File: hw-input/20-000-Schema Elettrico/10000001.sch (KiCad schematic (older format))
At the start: 32 parts

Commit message: Completamento sbroglio hw-output
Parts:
- removed IC? (x2): LTV-358T, MFSOP6, symbol LTV-358T
- added IC1, IC2: TLP291, SOP4, symbol TLP291
- gave numbers to parts that had none: 30
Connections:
- net labels removed: IO_1_L

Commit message: Aggiunte capacità di bypass su alimentazione I2C expander
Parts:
- added C1: 100n, Capacitors_SMD:C_0603, symbol C
- added C2: 1u, Capacitors_SMD:C_0603, symbol C
- IC1, IC2: footprint SOP4 -> (none)
- R1, R2, R3, R4, R5, R6, R7, R8, R9: footprint ~ -> Resistors_SMD:R_0603
- R10, R11, R12, R13, R14, R15, R16, R17, R18, R19: footprint ~ -> (none)
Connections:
- wire segments 115 -> 121
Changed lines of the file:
@@
 LIBS:optocoupler-2
 LIBS:10000001-cache
-EELAYER 27 0
+EELAYER 25 0
 EELAYER END
 $Descr A4 11693 8268
@@
 F 0 "R7" V 4450 1450 40  0000 C CNN
 F 1 "10000" V 4507 1251 40  0000 C CNN
-F 2 "~" V 4430 1250 30  0000 C CNN
+F 2 "Resistors_SMD:R_0603" V 4430 1250 30  0000 C CNN
 F 3 "~" H 4500 1250 30  0000 C CNN
 	1    4500 1250
@@
 F 0 "R8" V 4600 1450 40  0000 C CNN
 F 1 "10000" V 4657 1251 40  0000 C CNN
-F 2 "~" V 4580 1250 30  0000 C CNN
+F 2 "Resistors_SMD:R_0603" V 4580 1250 30  0000 C CNN
 F 3 "~" H 4650 1250 30  0000 C CNN
 	1    4650 1250
@@
 F 0 "R9" V 4750 1450 40  0000 C CNN
 F 1 "10000" V 4807 1251 40  0000 C CNN
-F 2 "~" V 4730 1250 30  0000 C CNN
+F 2 "Resistors_SMD:R_0603" V 4730 1250 30  0000 C CNN
 F 3 "~" H 4800 1250 30  0000 C CNN
 	1    4800 1250
@@
 F 0 "R6" V 2200 6500 40  0000 C CNN
 F 1 "0" V 2157 6701 40  0000 C CNN
-F 2 "~" V 2080 6700 30  0000 C CNN
+F 2 "Resistors_SMD:R_0603" V 2080 6700 30  0000 C CNN
 F 3 "~" H 2150 6700 30  0000 C CNN
 	1    2150 6700
@@
 F 0 "R5" V 2200 6400 40  0000 C CNN
 F 1 "0" V 2157 6601 40  0000 C CNN
-F 2 "~" V 2080 6600 30  0000 C CNN
+F 2 "Resistors_SMD:R_0603" V 2080 6600 30  0000 C CNN
 F 3 "~" H 2150 6600 30  0000 C CNN
 	1    2150 6600
@@
 F 0 "R4" V 2200 6300 40  0000 C CNN
 F 1 "0" V 2157 6501 40  0000 C CNN
-F 2 "~" V 2080 6500 30  0000 C CNN
+F 2 "Resistors_SMD:R_0603" V 2080 6500 30  0000 C CNN
 F 3 "~" H 2150 6500 30  0000 C CNN
 	1    2150 6500
@@
 F 0 "R3" V 2200 6200 40  0000 C CNN
 F 1 "0" V 2157 6401 40  0000 C CNN
-F 2 "~" V 2080 6400 30  0000 C CNN
+F 2 "Resistors_SMD:R_0603" V 2080 6400 30  0000 C CNN
 F 3 "~" H 2150 6400 30  0000 C CNN
 	1    2150 6400
@@
 F 0 "R2" V 2200 6100 40  0000 C CNN
 F 1 "0" V 2157 6301 40  0000 C CNN
-F 2 "~" V 2080 6300 30  0000 C CNN
+F 2 "Resistors_SMD:R_0603" V 2080 6300 30  0000 C CNN
 F 3 "~" H 2150 6300 30  0000 C CNN
 	1    2150 6300
@@
 F 0 "R1" V 2200 6000 40  0000 C CNN
 F 1 "0" V 2157 6201 40  0000 C CNN
-F 2 "~" V 2080 6200 30  0000 C CNN
+F 2 "Resistors_SMD:R_0603" V 2080 6200 30  0000 C CNN
 F 3 "~" H 2150 6200 30  0000 C CNN
 	1    2150 6200
@@
 F 0 "R17" V 7830 5750 40  0000 C CNN
 F 1 "2400" V 7757 5751 40  0000 C CNN
-F 2 "~" V 7680 5750 30  0000 C CNN
+F 2 "" V 7680 5750 30  0000 C CNN
 F 3 "~" H 7750 5750 30  0000 C CNN
 	1    7750 5750
@@
 F 0 "R19" V 8380 5750 40  0000 C CNN
 F 1 "2400" V 8307 5751 40  0000 C CNN
-F 2 "~" V 8230 5750 30  0000 C CNN
+F 2 "" V 8230 5750 30  0000 C CNN
 F 3 "~" H 8300 5750 30  0000 C CNN
 	1    8300 5750
@@
 F 0 "R15" V 7530 6050 40  0000 C CNN
 F 1 "100" V 7457 6051 40  0000 C CNN
-F 2 "~" V 7380 6050 30  0000 C CNN
+F 2 "" V 7380 6050 30  0000 C CNN
 F 3 "~" H 7450 6050 30  0000 C CNN
 	1    7450 6050
@@
 F 0 "R14" V 7530 4300 40  0000 C CNN
 F 1 "100" V 7457 4301 40  0000 C CNN
-F 2 "~" V 7380 4300 30  0000 C CNN
+F 2 "" V 7380 4300 30  0000 C CNN
 F 3 "~" H 7450 4300 30  0000 C CNN
 	1    7450 4300
@@
 F 0 "R18" V 8380 4000 40  0000 C CNN
 F 1 "2400" V 8307 4001 40  0000 C CNN
-F 2 "~" V 8230 4000 30  0000 C CNN
+F 2 "" V 8230 4000 30  0000 C CNN
 F 3 "~" H 8300 4000 30  0000 C CNN
 	1    8300 4000
@@
 F 0 "R16" V 7830 4000 40  0000 C CNN
 F 1 "2400" V 7757 4001 40  0000 C CNN
-F 2 "~" V 7680 4000 30  0000 C CNN
+F 2 "" V 7680 4000 30  0000 C CNN
 F 3 "~" H 7750 4000 30  0000 C CNN
 	1    7750 4000
@@
 F 0 "R12" V 6480 5450 40  0000 C CNN
 F 1 "1000" V 6407 5451 40  0000 C CNN
-F 2 "~" V 6330 5450 30  0000 C CNN
+F 2 "" V 6330 5450 30  0000 C CNN
 F 3 "~" H 6400 5450 30  0000 C CNN
 	1    6400 5450
@@
 F 0 "R13" V 6480 6050 40  0000 C CNN
 F 1 "10000" V 6407 6051 40  0000 C CNN
-F 2 "~" V 6330 6050 30  0000 C CNN
+F 2 "" V 6330 6050 30  0000 C CNN
 F 3 "~" H 6400 6050 30  0000 C CNN
 	1    6400 6050
@@
 F 0 "R11" V 6480 4300 40  0000 C CNN
 F 1 "10000" V 6407 4301 40  0000 C CNN
-F 2 "~" V 6330 4300 30  0000 C CNN
+F 2 "" V 6330 4300 30  0000 C CNN
 F 3 "~" H 6400 4300 30  0000 C CNN
 	1    6400 4300
@@
 F 0 "R10" V 6480 3700 40  0000 C CNN
 F 1 "1000" V 6407 3701 40  0000 C CNN
-F 2 "~" V 6330 3700 30  0000 C CNN
+F 2 "" V 6330 3700 30  0000 C CNN
 F 3 "~" H 6400 3700 30  0000 C CNN
 	1    6400 3700
@@
 F 0 "IC1" H 6787 4278 40  0000 C CNN
 F 1 "TLP291" H 7149 3916 40  0000 C CNN
-F 2 "SOP4" H 6836 3926 29  0000 C CNN
+F 2 "" H 6836 3926 29  0000 C CNN
 F 3 "" H 7000 4100 60  0000 C CNN
 	1    7000 4100
@@
 F 0 "IC2" H 6787 6028 40  0000 C CNN
 F 1 "TLP291" H 7149 5666 40  0000 C CNN
-F 2 "SOP4" H 6836 5676 29  0000 C CNN
+F 2 "" H 6836 5676 29  0000 C CNN
 F 3 "" H 7000 5850 60  0000 C CNN
 	1    7000 5850
 	-1   0    0    -1
 $EndComp
+$Comp
+L C C2
+U 1 1 55357ECE
+P 3200 1200
+F 0 "C2" H 3250 1300 50  0000 L CNN
+F 1 "1u" H 3250 1100 50  0000 L CNN
+F 2 "Capacitors_SMD:C_0603" H 3238 1050 30  0001 C CNN
+F 3 "" H 3200 1200 60  0000 C CNN
+	1    3200 1200
+	1    0    0    -1
+$EndComp
+$Comp
+L C C1
+U 1 1 55357FCD
+P 2900 1200
+F 0 "C1" H 2950 1300 50  0000 L CNN
+F 1 "100n" H 2950 1100 50  0000 L CNN
+F 2 "Capacitors_SMD:C_0603" H 2938 1050 30  0001 C CNN
+F 3 "" H 2900 1200 60  0000 C CNN
+	1    2900 1200
+	1    0    0    -1
+$EndComp
+$Comp
+L GND #PWR017
+U 1 1 5535805C
+P 2900 1550
+F 0 "#PWR017" H 2900 1550 30  0001 C CNN
+F 1 "GND" H 2900 1480 30  0001 C CNN
+F 2 "" H 2900 1550 60  0001 C CNN
+F 3 "" H 2900 1550 60  0001 C CNN
+	1    2900 1550
+	1    0    0    -1
+$EndComp
+$Comp
+L VDD #PWR018
+U 1 1 55358089
+P 2900 800
+F 0 "#PWR018" H 2900 900 30  0001 C CNN
+F 1 "VDD" H 2900 910 30  0000 C CNN
+F 2 "" H 2900 800 60  0001 C CNN
+F 3 "" H 2900 800 60  0001 C CNN
+	1    2900 800
+	1    0    0    -1
+$EndComp
+Wire Wire Line
+	2900 800  2900 1000
+Wire Wire Line
+	2900 900  3200 900
+Wire Wire Line
+	3200 900  3200 1000
+Connection ~ 2900 900
+Wire Wire Line
+	2900 1400 2900 1550
+Wire Wire Line
+	2900 1500 3200 1500
+Wire Wire Line
+	3200 1500 3200 1400
+Connection ~ 2900 1500
 $EndSCHEMATC

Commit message: Aggiornato schema scheda temperatura a nuova versione kicad. Aggiunti script e librerie per generazione diretta BOM con codici d'ordine.
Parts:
- C1, C2: symbol C -> C-RESCUE-10000001
- D1, D2: symbol ZENERSMALL -> ZENERsmall
- IC1, IC2: symbol TLP291 -> TLP291-RESCUE-10000001
- R1, R10, R11, R12, R13, R14, R15, R16, R17, R18, R19, R2, R3, R4, R5, R6, R7, R8, R9: symbol R -> R-RESCUE-10000001
- U1: symbol PCF8574 -> PCF8574-RESCUE-10000001
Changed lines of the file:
@@
 EESchema Schematic File Version 2
+LIBS:10000001-rescue
 LIBS:opto
 LIBS:power
@@
 LIBS:memory
 LIBS:xilinx
-LIBS:special
 LIBS:microcontrollers
 LIBS:dsp
@@
 LIBS:contrib
 LIBS:valves
-LIBS:AQZ204
 LIBS:ftdi
-LIBS:optocoupler
-LIBS:optocoupler-2
 LIBS:10000001-cache
 EELAYER 25 0
@@
 	9800 6100 9800 6150
 $Comp
-L ZENERSMALL D2
+L ZENERsmall D2
 U 1 1 547BA3D0
 P 9800 6250
@@
 IO_0_P
 $Comp
-L ZENERSMALL D1
+L ZENERsmall D1
 U 1 1 547BA3A6
 P 9800 5800
@@
 I2C_SCL
 $Comp
-L R R7
+L R-RESCUE-10000001 R7
 U 1 1 547BA201
 P 4500 1250
@@
 $EndComp
 $Comp
-L R R8
+L R-RESCUE-10000001 R8
 U 1 1 547BA1FE
 P 4650 1250
@@
 $EndComp
 $Comp
-L R R9
+L R-RESCUE-10000001 R9
 U 1 1 547BA1E9
 P 4800 1250
@@
 $EndComp
 $Comp
-L PCF8574 U1
+L PCF8574-RESCUE-10000001 U1
 U 1 1 547BA1C7
 P 5800 2000
@@
 IO_1_CMD
 $Comp
-L R R6
+L R-RESCUE-10000001 R6
 U 1 1 547BA02B
 P 2150 6700
@@
 $EndComp
 $Comp
-L R R5
+L R-RESCUE-10000001 R5
 U 1 1 547BA026
 P 2150 6600
@@
 $EndComp
 $Comp
-L R R4
+L R-RESCUE-10000001 R4
 U 1 1 547BA01C
 P 2150 6500
@@
 $EndComp
 $Comp
-L R R3
+L R-RESCUE-10000001 R3
 U 1 1 547BA018
 P 2150 6400
@@
 $EndComp
 $Comp
-L R R2
+L R-RESCUE-10000001 R2
 U 1 1 547B9FFD
 P 2150 6300
@@
 $EndComp
 $Comp
-L R R1
+L R-RESCUE-10000001 R1
 U 1 1 547B9FF3
 P 2150 6200
@@
 IO_1_N
 $Comp
-L R R17
+L R-RESCUE-10000001 R17
 U 1 1 547B9E50
 P 7750 5750
@@
 $EndComp
 $Comp
-L R R19
+L R-RESCUE-10000001 R19
 U 1 1 547B9E4F
 P 8300 5750
@@
 $EndComp
 $Comp
-L R R15
+L R-RESCUE-10000001 R15
 U 1 1 547B9E4E
 P 7450 6050
@@
 $EndComp
 $Comp
-L R R14
+L R-RESCUE-10000001 R14
 U 1 1 547B9DEF
 P 7450 4300
@@
 $EndComp
 $Comp
-L R R18
+L R-RESCUE-10000001 R18
 U 1 1 547B9DDC
 P 8300 4000
@@
 $EndComp
 $Comp
-L R R16
+L R-RESCUE-10000001 R16
 U 1 1 547B9DBB
 P 7750 4000
@@
 $EndComp
 $Comp
-L R R12
+L R-RESCUE-10000001 R12
 U 1 1 547B9BC6
 P 6400 5450
@@
 $EndComp
 $Comp
-L R R13
+L R-RESCUE-10000001 R13
 U 1 1 547B9BC3
 P 6400 6050
@@
 $EndComp
 $Comp
-L R R11
+L R-RESCUE-10000001 R11
 U 1 1 547B9AAC
 P 6400 4300
@@
 IO_1_N
 $Comp
-L R R10
+L R-RESCUE-10000001 R10
 U 1 1 5456065C
 P 6400 3700
@@
 Protezioni lato utente
 $Comp
-L TLP291 IC1
+L TLP291-RESCUE-10000001 IC1
 U 1 1 54E9B476
 P 7000 4100
@@
 $EndComp
 $Comp
-L TLP291 IC2
+L TLP291-RESCUE-10000001 IC2
 U 1 1 54E9B4A1
 P 7000 5850
@@
 $EndComp
 $Comp
-L C C2
+L C-RESCUE-10000001 C2
 U 1 1 55357ECE
 P 3200 1200
@@
 $EndComp
 $Comp
-L C C1
+L C-RESCUE-10000001 C1
 U 1 1 55357FCD
 P 2900 1200

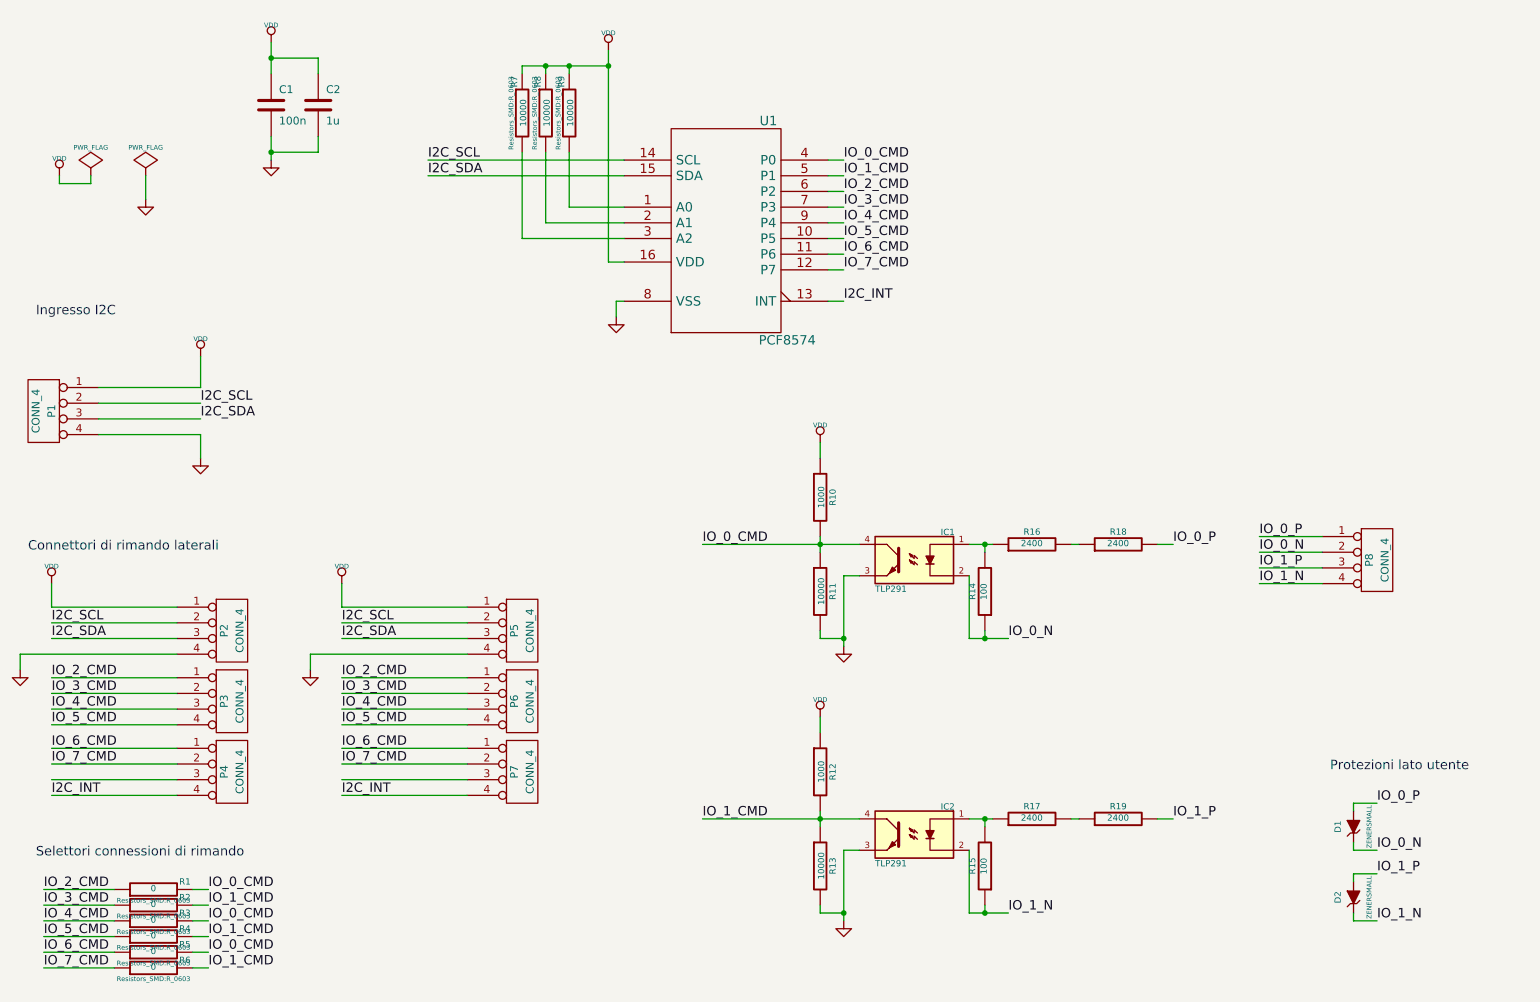
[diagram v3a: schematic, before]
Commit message: Completato schema elettrico con codice produttore
Signed-off-by: CrazyDiamond <crazyd14@gmail.com>
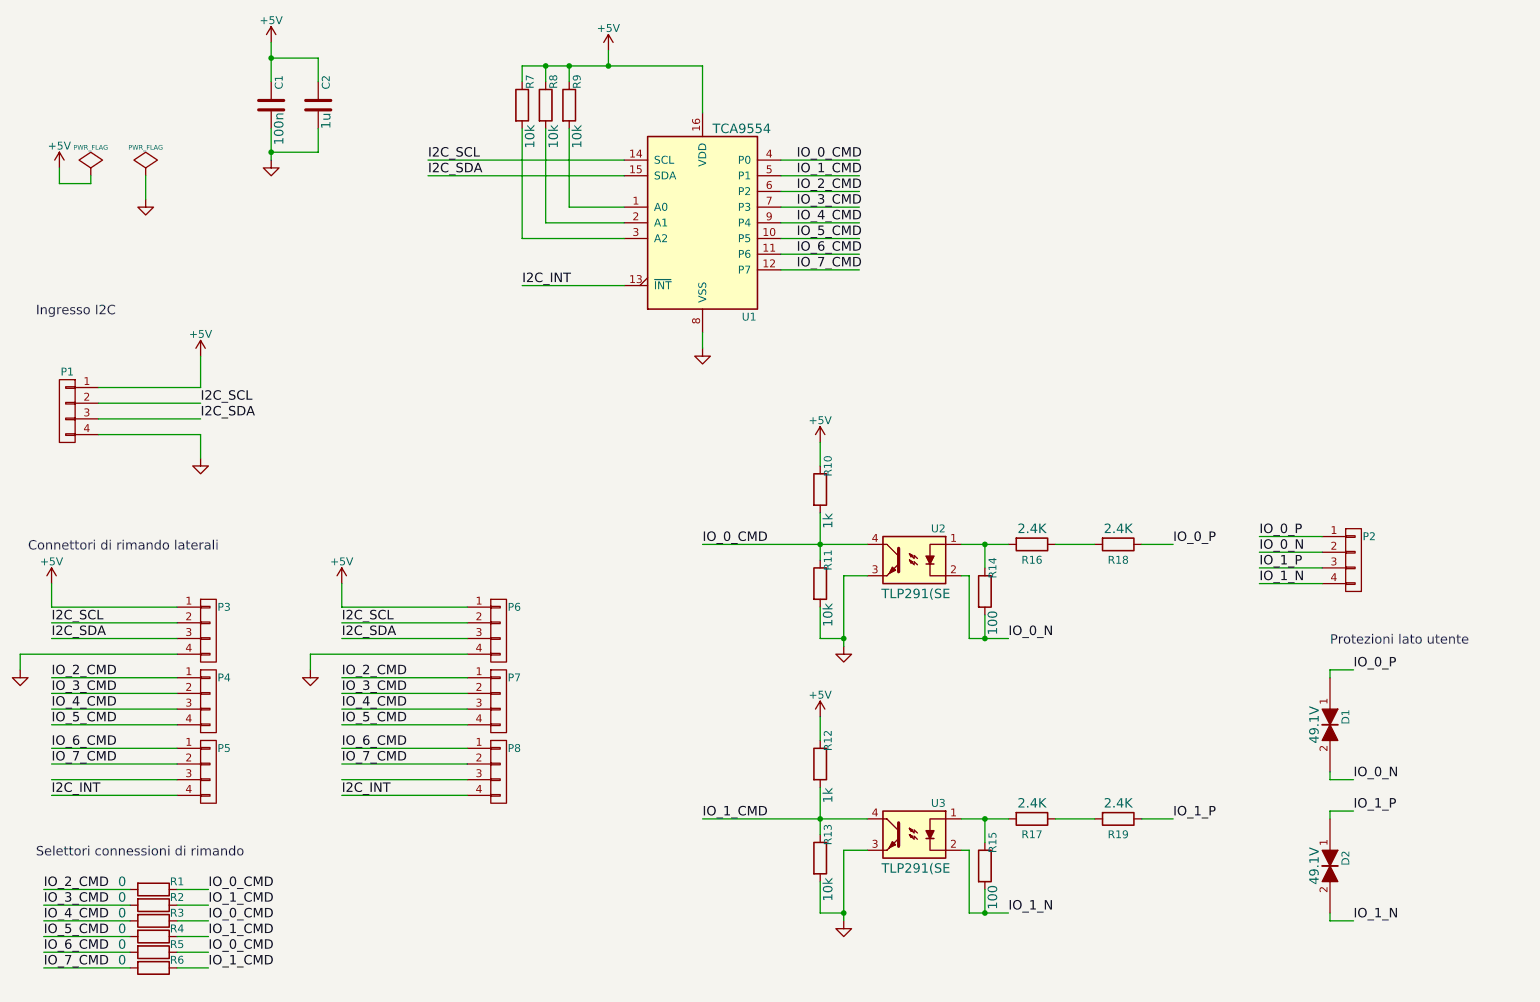
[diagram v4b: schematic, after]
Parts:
- removed C1: 100n, Capacitors_SMD:C_0603, symbol C-RESCUE-10000001
- removed C2: 1u, Capacitors_SMD:C_0603, symbol C-RESCUE-10000001
- removed D1, D2: ZENERSMALL, symbol ZENERsmall
- removed IC1, IC2: TLP291, symbol TLP291-RESCUE-10000001
- removed P1, P2, P3, P4, P5, P6, P7, P8: CONN_4, symbol CONN_4
- removed R1, R2, R3, R4, R5, R6: 0, Resistors_SMD:R_0603, symbol R-RESCUE-10000001
- removed R10, R12: 1000, symbol R-RESCUE-10000001
- removed R11, R13: 10000, symbol R-RESCUE-10000001
- removed R14, R15: 100, symbol R-RESCUE-10000001
- removed R16, R17, R18, R19: 2400, symbol R-RESCUE-10000001
- removed R7, R8, R9: 10000, Resistors_SMD:R_0603, symbol R-RESCUE-10000001
- removed U1: PCF8574, symbol PCF8574-RESCUE-10000001
- added C1: C_100n_0603_10_X7R_25V, Capacitors_SMD:C_0603, symbol C_100n_0603_10_X7R_25V
- added C2: C_1u_0603_10_X7R_25V, Capacitors_SMD:C_0603, symbol C_1u_0603_10_X7R_25V
- added D1, D2: TVS_SMC_49.1V, Diodes_SMD:SMC_Standard, symbol TVS_SMC_49.1V
- added P1, P2, P3, P4, P5, P6, P7, P8: PLUG_01X04_254, Socket_Strips:Socket_Strip_Straight_1x04, symbol PLUG_01X04_254
- added R1, R2, R3, R4, R5, R6: R_0_0603_5, Resistors_SMD:R_0603, symbol R_0_0603_5
- added R10, R12: R_1K_0603_5, Resistors_SMD:R_0603, symbol R_1K_0603_5
- added R11, R13, R7, R8, R9: R_10K_0603_5, Resistors_SMD:R_0603, symbol R_10K_0603_5
- added R15, R?: R_100_0603_5, Resistors_SMD:R_0603, symbol R_100_0603_5
- added R17, R18, R19, R?: R_2K4_1206_5, Resistors_SMD:R_1206, symbol R_2K4_1206_5
- added U1: TCA9554, Housings_SSOP:SSOP-16_3.9x4.9mm_Pitch0.635mm, symbol TCA9554
- added U2, U3: TLP291(SE, os_optocoupler:TLP291, symbol TLP291(SE
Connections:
- net labels added: +5V
- net labels removed: VDD
- wire segments 121 -> 122

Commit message: Completato schema elettrico con codici produttore
Signed-off-by: CrazyDiamond <crazyd14@gmail.com>
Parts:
- gave numbers to parts that had none: 2
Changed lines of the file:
@@
 $EndComp
 $Comp
-L R_2K4_1206_5 R?
+L R_2K4_1206_5 R16
 U 1 1 57C97AC5
 P 7750 4000
@@
 $EndComp
 $Comp
-L R_100_0603_5 R?
+L R_100_0603_5 R14
 U 1 1 57C9816C
 P 7450 4300
